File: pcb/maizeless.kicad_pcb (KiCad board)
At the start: 2 copper layers, 129.8 x 90 mm, 26 parts, among them SW1 SW_PUSH, SW10 SW_PUSH, SW11 SW_PUSH, SW12 SW_PUSH, SW13 SW_PUSH, SW14 SW_PUSH, SW15 SW_PUSH, SW16 SW_PUSH, SW17 SW_PUSH, SW18 SW_PUSH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

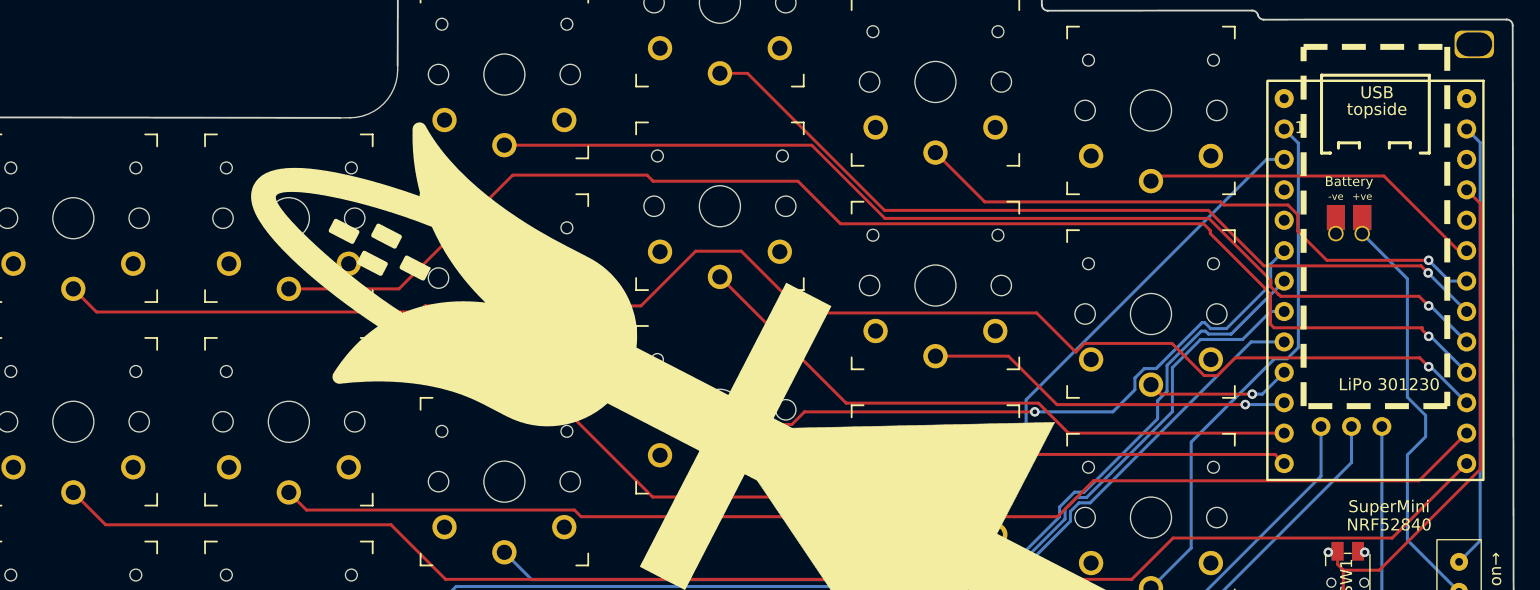
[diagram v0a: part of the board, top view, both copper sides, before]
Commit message: Re-route for nicer looking traces; fix missing ground
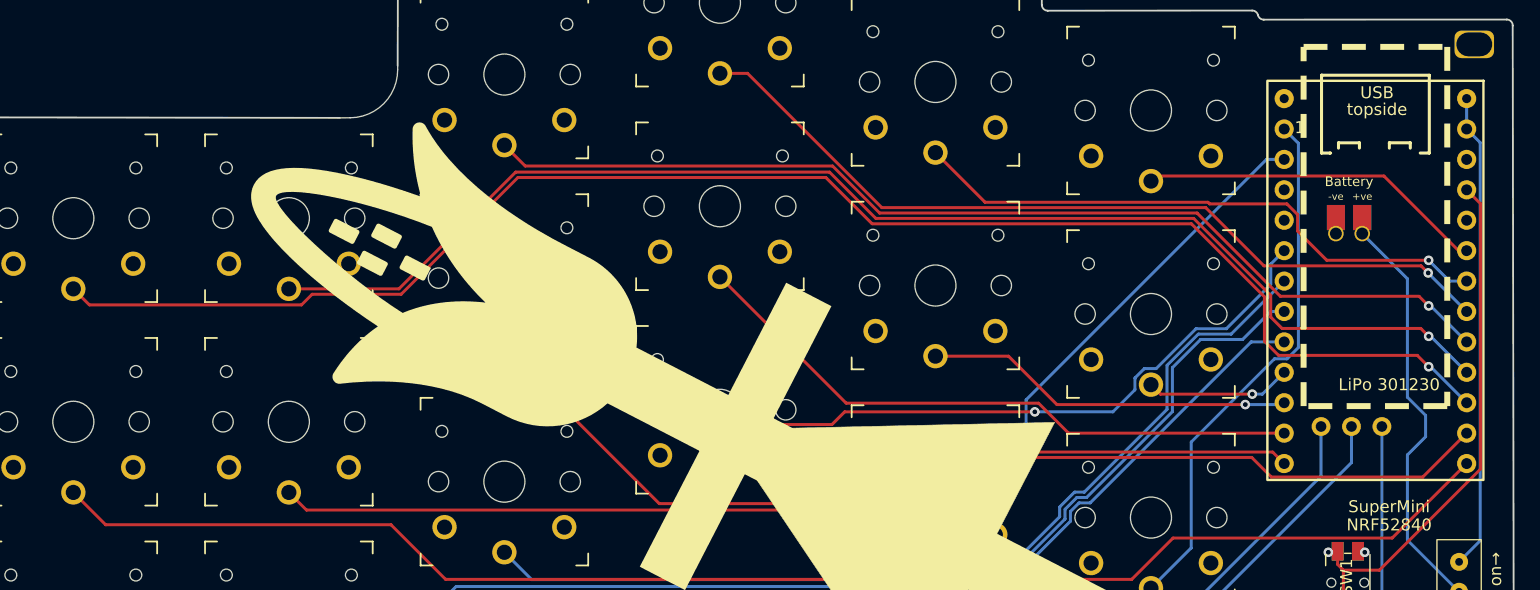
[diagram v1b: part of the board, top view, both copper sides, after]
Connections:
- u1 pad 28: unconnected-(u1-GND-Pad28) -> GND
- u1 pad 29: unconnected-(u1-BAT+-Pad29) -> vbat
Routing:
- net key1: track 126.3 -> 131.3 mm
- net vbat: track 37.3 -> 39.9 mm
- net key16: track 58.2 -> 56.7 mm
- net key8: track 102.1 -> 103.0 mm
- net key9: track 72.0 -> 72.7 mm

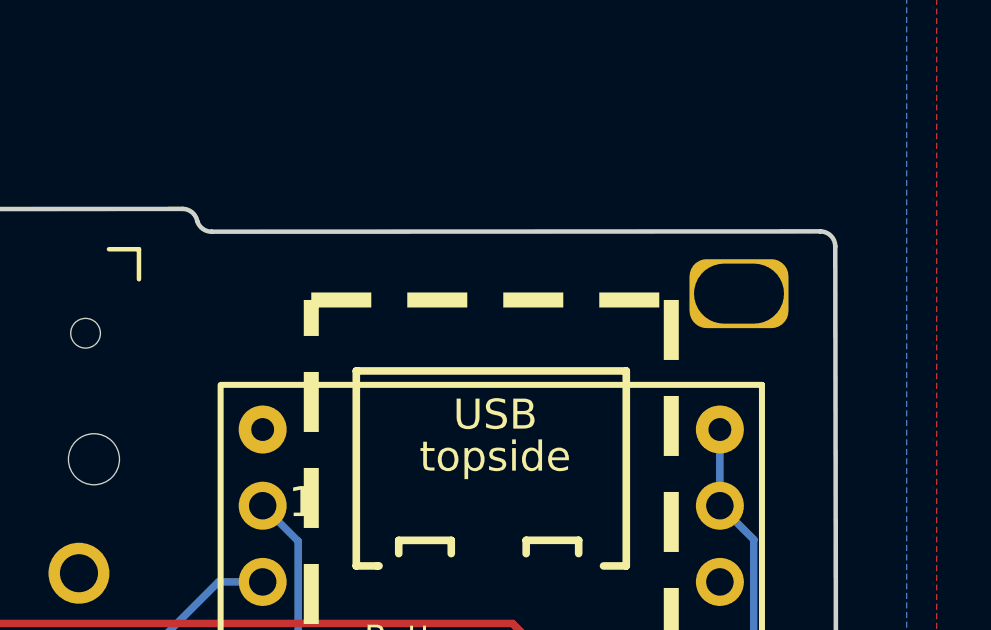
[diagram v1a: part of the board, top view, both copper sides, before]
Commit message: Extra battery pads in case I want to keep everything on top
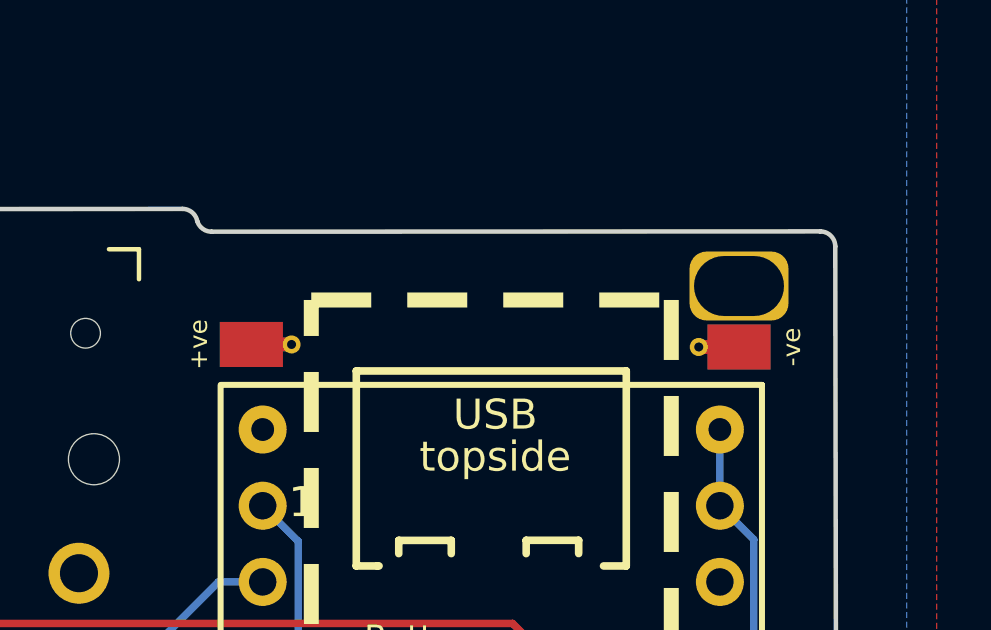
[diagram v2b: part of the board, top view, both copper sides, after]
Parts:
- added BT1: Battery_Cell, dumta:Battery_pads_reversible, F.Cu at (168.7, 58.7)
- added BT1: Battery_Cell, dumta:Battery_pads_reversible, F.Cu at (184.9, 58.8)
- moved REF** 0.25 mm to (184.9, 55.6)
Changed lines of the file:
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@@
   )
   (footprint "lib:routing_via" (layer "F.Cu")
-    (at 184.912 55.88)
+    (at 184.912 55.626)
     (attr through_hole)
     (fp_text reference "REF**" (at 0 -0.5 unlocked) (layer "F.SilkS") hide
@@
     )
   )
+  (footprint "dumta:Battery_pads_reversible" (layer "F.Cu")
+    (at 168.656 58.674 -90)
+    (property "Sheetfile" "maizeless.kicad_sch")
+    (property "Sheetname" "")
+    (property "ki_description" "Single-cell battery")
+    (property "ki_keywords" "battery cell")
+    (fp_text reference "BT1" (at 0 0.5 90) (layer "F.SilkS") hide
+        (effects (font (size 1 1) (thickness 0.15)))
+    )
+    (fp_text value "Battery_Cell" (at 0 -0.5 90) (layer "F.Fab") hide
+        (effects (font (size 1 1) (thickness 0.15)))
+    )
+    (fp_text user "+ve" (at -1.1 1.757 90) (layer "F.SilkS")
+        (effects (font (size 0.6 0.6) (thickness 0.08)))
+    )
+    (fp_poly
+      (pts
+        (xy -1.8 -1)
+        (xy -1.8 1)
+        (xy -0.4 1)
+        (xy -0.4 -1)
+      )
+      (stroke (width 0.1) (type solid)) (fill solid) (layer "B.Mask"))
+    (fp_poly
+      (pts
+        (xy -0.401442 -1)
+        (xy -0.401442 1)
+        (xy -1.801442 1)
+        (xy -1.801442 -1)
+      )
+      (stroke (width 0.1) (type solid)) (fill solid) (layer "F.Mask"))
+    (pad "1" thru_hole circle (at -1.1004 -1.3416 270) (size 0.6 0.6) (drill 0.3) (layers "*.Cu")
+      (pinfunction "+") (pintype "passive"))
+    (pad "1" smd custom (at -1.1 0 90) (size 1.5 2.1) (layers "F.Cu")
+      (pinfunction "+") (pintype "passive") (thermal_bridge_angle 45)
+      (options (clearance outline) (anchor rect))
+      (primitives
+        (gr_poly
+          (pts
+            (xy 0.179 1.3352)
+            (xy -0.1766 1.3352)
+            (xy -0.1766 0.762)
+            (xy 0.179 0.762)
+          )
+          (width 0.1) (fill yes))
+      ))
+    (pad "1" smd custom (at -1.1 0 270) (size 1.5 2.1) (layers "B.Cu")
+      (pinfunction "+") (pintype "passive") (thermal_bridge_angle 45)
+      (options (clearance outline) (anchor rect))
+      (primitives
+        (gr_poly
+          (pts
+            (xy 0.176556 -0.7618)
+            (xy -0.179044 -0.7618)
+            (xy -0.179044 -1.335)
+            (xy 0.176556 -1.335)
+          )
+          (width 0.1) (fill yes))
+      ))
+  )
   (footprint "lib:SW_PG1350_reversible" (layer "F.Cu")
     (at 67.91 87.4)
@@
       (net 1 "GND") (pinfunction "2") (pintype "passive"))
   )
+  (footprint "dumta:Battery_pads_reversible" (layer "F.Cu")
+    (at 184.912 58.758 90)
+    (property "Sheetfile" "maizeless.kicad_sch")
+    (property "Sheetname" "")
+    (property "ki_description" "Single-cell battery")
+    (property "ki_keywords" "battery cell")
+    (fp_text reference "BT1" (at 0 0.5 90) (layer "F.SilkS") hide
+        (effects (font (size 1 1) (thickness 0.15)))
+    )
+    (fp_text value "Battery_Cell" (at 0 -0.5 90) (layer "F.Fab") hide
+        (effects (font (size 1 1) (thickness 0.15)))
+    )
+    (fp_text user "-ve" (at 1.1 1.757 90) (layer "F.SilkS")
+        (effects (font (size 0.6 0.6) (thickness 0.08)))
+    )
+    (fp_poly
+      (pts
+        (xy 0.4 -1)
+        (xy 0.4 1)
+        (xy 1.8 1)
+        (xy 1.8 -1)
+      )
+      (stroke (width 0.1) (type solid)) (fill solid) (layer "B.Mask"))
+    (fp_poly
+      (pts
+        (xy 1.8 -1)
+        (xy 1.8 1)
+        (xy 0.4 1)
+        (xy 0.4 -1)
+      )
+      (stroke (width 0.1) (type solid)) (fill solid) (layer "F.Mask"))
+    (pad "2" thru_hole circle (at 1.1 -1.3416 90) (size 0.6 0.6) (drill 0.3) (layers "*.Cu")
+      (net 1 "GND") (pinfunction "-") (pintype "passive"))
+    (pad "2" smd custom (at 1.1 0 270) (size 1.5 2.1) (layers "F.Cu")
+      (net 1 "GND") (pinfunction "-") (pintype "passive") (thermal_bridge_angle 45)
+      (options (clearance outline) (anchor rect))
+      (primitives
+        (gr_poly
+          (pts
+            (xy 0.1786 1.3352)
+            (xy -0.177 1.3352)
+            (xy -0.177 0.762)
+            (xy 0.1786 0.762)
+          )
+          (width 0.1) (fill yes))
+      ))
+    (pad "2" smd custom (at 1.1 0 90) (size 1.5 2.1) (layers "B.Cu")
+      (net 1 "GND") (pinfunction "-") (pintype "passive") (thermal_bridge_angle 45)
+      (options (clearance outline) (anchor rect))
+      (primitives
+        (gr_poly
+          (pts
+            (xy 0.1766 -0.7618)
+            (xy -0.179 -0.7618)
+            (xy -0.179 -1.335)
+            (xy 0.1766 -1.335)
+          )
+          (width 0.1) (fill yes))
+      ))
+  )
   (footprint "lib:SW_PG1350_reversible" (layer "F.Cu")
